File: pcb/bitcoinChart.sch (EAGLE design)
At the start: 2 parts

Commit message: Added components
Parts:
- removed U$1: PINHD-1X10, adafruit:PINHD-1X10
- added C1: (no value), resistor:C-EUC1206K
- added C6, C7: 10uF, basic_components:SMD-CAPACITOR0805
- added D1: GREEN, SparkFun-LED:LED-GREEN1206
- added D13, D14: 1n4148, basic_components:DIODESOD-323
- added D15, D16: MBR120, basic_components:DIODE-SCHOTTKYSOD-123
- added D17: RED, basic_components:LED
- added D2: RED, SparkFun-LED:LED-RED1206
- added R1, R2: (no value), resistor:R-EU_M1206
- added R15, R16, R17, R18, R19: 10K, basic_components:SMD-RESISTORR0805
- added R20: 1K, basic_components:SMD-RESISTORR0805
- added S1, S2, S3: MOMENTARY-SWITCH-SPST-PTH-6.0MM-KIT, SparkFun-Switches:MOMENTARY-SWITCH-SPST-PTH-6.0MM-KIT
- added SV1: (no value), untitled:FE10-1
- added SW5, SW6: KMR2, basic_components:BUTTON_KMR2KMR2
- added U$42: CONN-1X6, basic_components:CONN-1X6
- added U2: MPU-6050, MPU-6050:MPU-6050
- added U7: SPX3819, basic_components:MIC5219SOT-23-5
- added U8: (no value), basic_components:ESP12ESMD
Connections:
- removed net N$13: B1.D8, U$1.8
- new net +3.3V: B1.3.3V, U2.VDD
- new net 3.3V: C6.1, D17.A, R15.2, R16.2, R19.2, U7.OUT, U8.VCC
- new net ADC: U8.ADC
- new net CH_PD: R15.1, U8.CH_PD
- new net CS0: U8.CS0
- new net GPIO0: R20.1, SW6.S, SW6.S1, U8.GPIO0
- new net GPIO10: U8.*GPIO10
- new net GPIO12: U8.GPIO12
- new net GPIO13: U8.GPIO13
- new net GPIO14: U8.GPIO14
- new net GPIO15: R17.2, U8.GPIO15
- new net GPIO16: U8.GPIO16
- new net GPIO2: R19.1, U8.GPIO2
- new net GPIO4: U8.GPIO4
- new net GPIO5: U8.GPIO5
- new net GPIO9: U8.*GPIO9
- new net LDO_EN: R18.2, U7.EN
- new net MISO: U8.MISO
- new net MOSI: U8.MOSI
- new net N$1: SV1.2
- new net N$14: C7.1, D15.C, D16.C, R18.1, U7.IN
- new net N$15: D17.C, R20.2
- new net N$2: B1.A5, U2.SCL
- new net N$3: B1.A4, U2.SDA
- new net N$5: B1.D8, SV1.3
- new net RESET: D13.A, R16.1, SW5.S, SW5.S1, U8.RESET
- new net RESET_5V: D13.C
- new net RXD: B1.TX, D14.A, U8.RX
- new net RXD_5V: D14.C, U$42.3
- new net SCLK: U8.SCLK
- new net TXD: B1.RX, U$42.2, U8.TX
- new net VBAT: D16.A
- new net VIN: U$42.4
- net +5V: now also D15.A, SV1.5; no longer U$1.6, U$1.9
- net GND: now also B1.GND@0, B1.GND@1, B1.GND@2, C6.2, C7.2, R17.1, SV1.1, SW5.P, SW5.P1, SW6.P, SW6.P1, U$42.6, U2.GND, U7.GND, U8.GND; no longer U$1.10
- net N$4: now also SV1.10; no longer U$1.1
- net N$6: now also SV1.8; no longer U$1.3
- net N$7: now also SV1.7; no longer U$1.4
- net N$8: now also SV1.6; no longer U$1.5
- net N$9: now also SV1.4; no longer U$1.7

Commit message: Completed PCB
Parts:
- added C2, C4: 0.1uF, resistor:C-EUC1206K
- added C3: 10nF, resistor:C-EUC1206K
- added R3, R4, R5: 10k, resistor:R-EU_M1206
- C1: value (none) -> 2.2nF
- S1, S2, S3: value MOMENTARY-SWITCH-SPST-PTH-6.0MM-KIT -> MOMENTARY-SWITCH-SPST-SMD-6.2MM-TALL; device SparkFun-Switches:MOMENTARY-SWITCH-SPST-PTH-6.0MM-KIT -> SparkFun-Switches:MOMENTARY-SWITCH-SPST-SMD-6.2MM-TALL
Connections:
- new net LED_G: B1.*D5, R1.1
- new net LED_R: B1.*D6, R2.1
- new net N$10: C2.2, U2.REGOUT
- new net N$11: C1.2, U2.CPOUT
- new net N$12: C3.2, U2.VLOGIC
- new net N$13: D1.A, R1.2
- new net N$16: D2.A, R2.2
- new net SW1: B1.D2, R3.1, S1.1
- new net SW2: B1.D4, R4.1, S2.1
- new net SW3: B1.D7, R5.1, S3.1
- net +3.3V: now also C4.2
- net +5V: now also R3.2, R4.2, R5.2
- net GND: now also C1.1, C2.1, C3.1, C4.1, D1.C, D2.C, S1.2, S2.2, S3.2
- net N$2: now also B1.SCL; no longer B1.A5
- net N$3: now also B1.SDA; no longer B1.A4
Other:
- moved on the sheet: B1, C1, C6, C7, D1, D13, D14, D15, D16, D17, D2, R1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

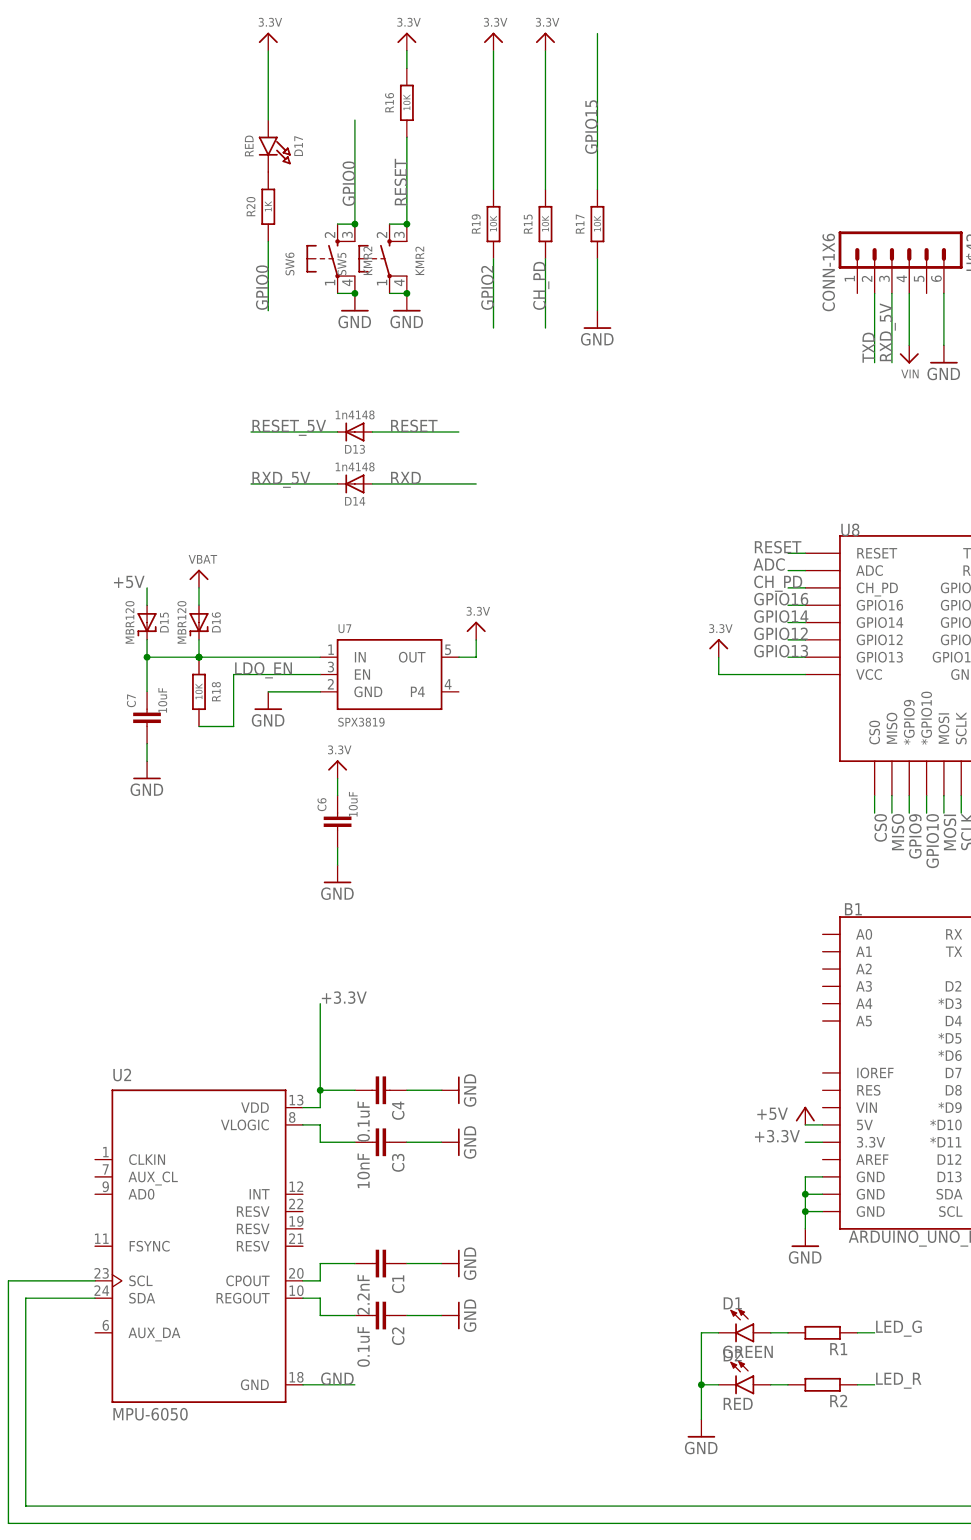
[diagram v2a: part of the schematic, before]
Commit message: Changed LED package, removed routing over antenna
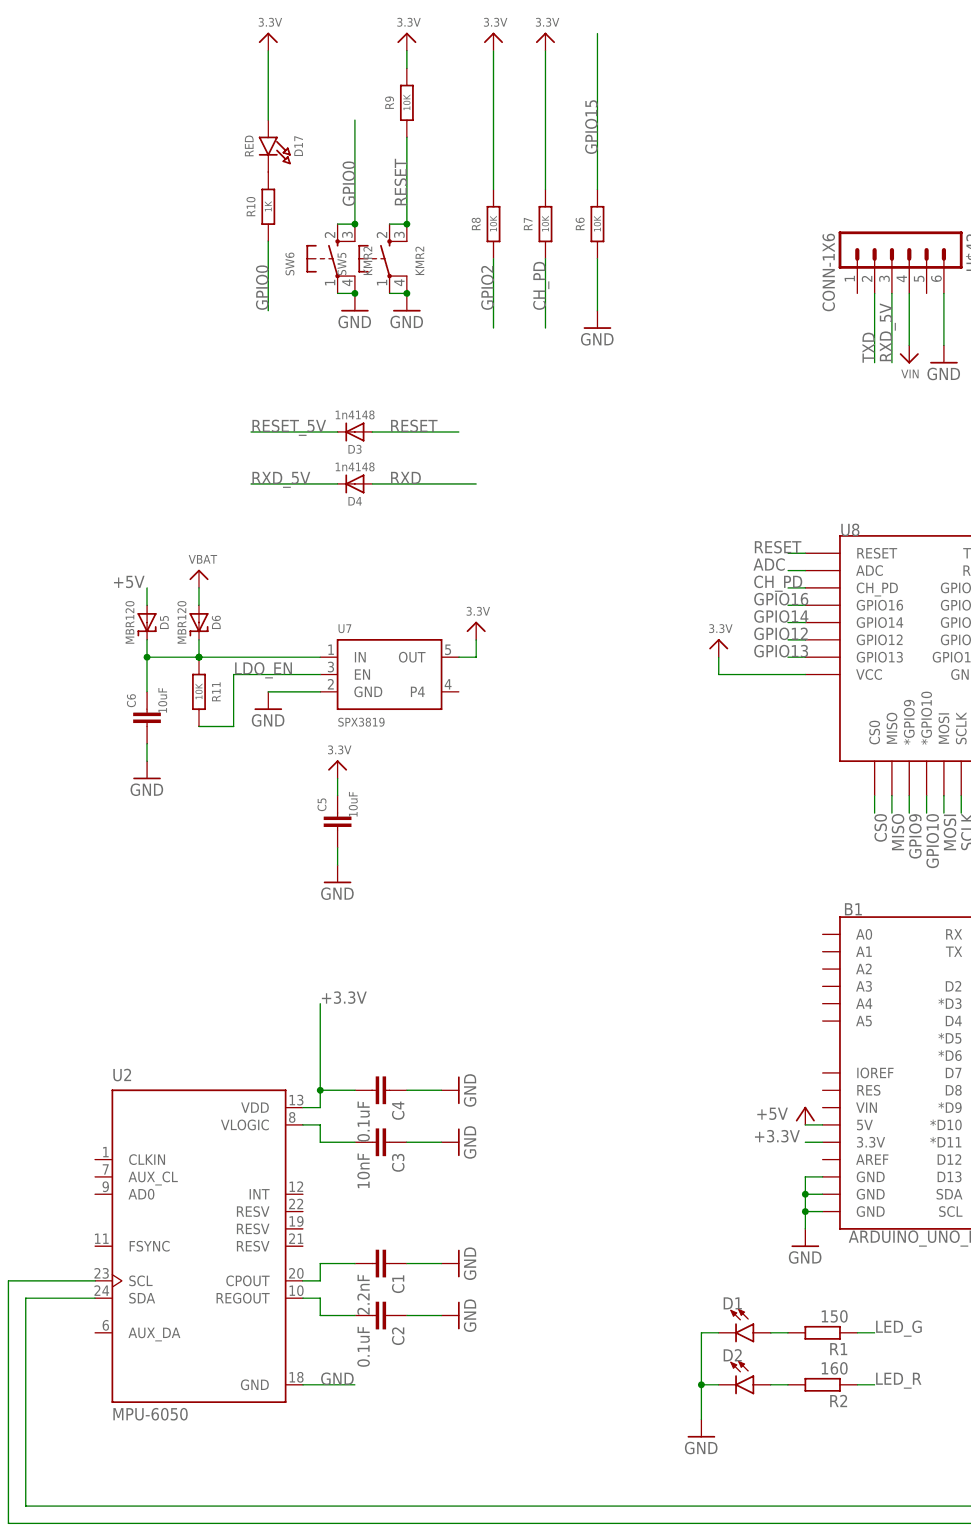
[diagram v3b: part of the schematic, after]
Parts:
- removed C7: 10uF, basic_components:SMD-CAPACITOR0805
- added C5: 10uF, basic_components:SMD-CAPACITOR0805
- D1: device SparkFun-LED:LED-GREEN1206 -> led:LEDCHIPLED_0805
- D2: device SparkFun-LED:LED-RED1206 -> led:LEDCHIPLED_0805
- R1: value (none) -> 150
- R2: value (none) -> 160
- renumbered D13 to D3, D14 to D4, D15 to D5, D16 to D6, R15 to R7, R16 to R9, R17 to R6, R18 to R11, R19 to R8, R20 to R10
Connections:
- net 3.3V: now also C5.1; no longer C6.1
- net GND: now also C5.2; no longer C7.2
- net N$14: now also C6.1; no longer C7.1
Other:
- moved on the sheet: C6

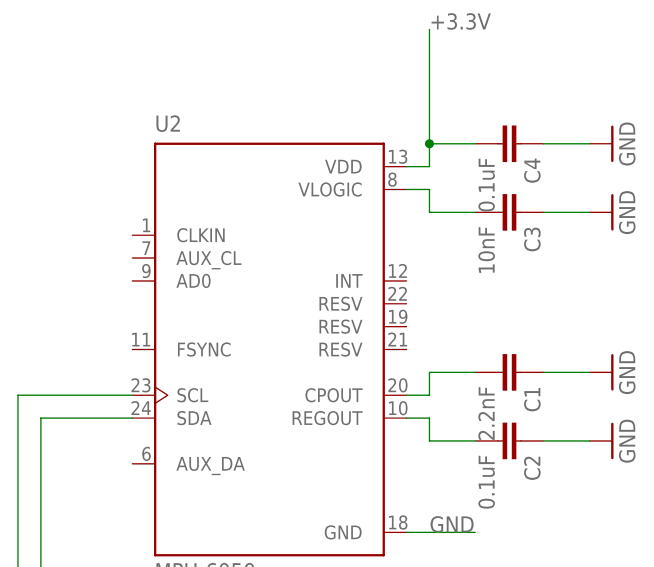
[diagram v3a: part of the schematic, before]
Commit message: Picture, connected some pins on MPU6050
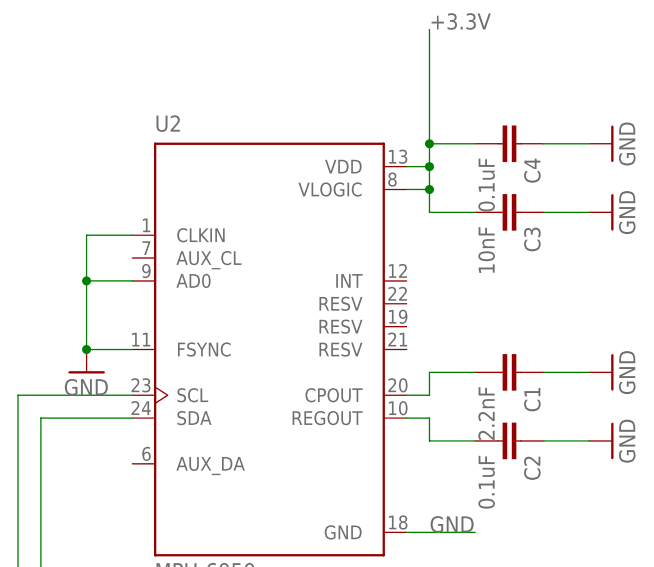
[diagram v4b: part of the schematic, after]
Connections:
- removed net N$12: C3.2, U2.VLOGIC
- net +3.3V: now also C3.2, U2.VLOGIC
- net GND: now also U2.AD0, U2.CLKIN, U2.FSYNC
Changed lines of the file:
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@@
 </class>
 <class number="1" name="test" width="0.1524" drill="0.4">
-<clearance class="1" value="0.3"/>
 </class>
 <class number="2" name="3v" width="0.1524" drill="0.3">
@@
 <part name="GND7" library="supply1" library_urn="urn:adsk.eagle:library:371" deviceset="GND" device=""/>
 <part name="FRAME1" library="frames" library_urn="urn:adsk.eagle:library:229" deviceset="A3L-LOC" device=""/>
+<part name="GND8" library="supply1" library_urn="urn:adsk.eagle:library:371" deviceset="GND" device=""/>
 </parts>
 <sheets>
@@
 <attribute name="SHEET" x="357.505" y="5.08" size="2.54" layer="94"/>
 </instance>
+<instance part="GND8" gate="1" x="48.26" y="60.96" smashed="yes">
+<attribute name="VALUE" x="45.72" y="58.42" size="1.778" layer="96"/>
+</instance>
 </instances>
 <busses>
@@
 <wire x1="248.92" y1="33.02" x2="248.92" y2="40.64" width="0.1524" layer="91"/>
 <junction x="248.92" y="33.02"/>
+</segment>
+<segment>
+<pinref part="U2" gate="G$1" pin="CLKIN"/>
+<wire x1="53.34" y1="76.2" x2="48.26" y2="76.2" width="0.1524" layer="91"/>
+<pinref part="GND8" gate="1" pin="GND"/>
+<wire x1="48.26" y1="76.2" x2="48.26" y2="71.12" width="0.1524" layer="91"/>
+<pinref part="U2" gate="G$1" pin="AD0"/>
+<wire x1="48.26" y1="71.12" x2="48.26" y2="63.5" width="0.1524" layer="91"/>
+<wire x1="53.34" y1="71.12" x2="48.26" y2="71.12" width="0.1524" layer="91"/>
+<junction x="48.26" y="71.12"/>
+<pinref part="U2" gate="G$1" pin="FSYNC"/>
+<wire x1="53.34" y1="63.5" x2="48.26" y2="63.5" width="0.1524" layer="91"/>
+<junction x="48.26" y="63.5"/>
 </segment>
 </net>
@@
 <wire x1="86.36" y1="86.36" x2="91.44" y2="86.36" width="0.1524" layer="91"/>
 <junction x="86.36" y="86.36"/>
+<pinref part="U2" gate="G$1" pin="VLOGIC"/>
+<wire x1="83.82" y1="81.28" x2="86.36" y2="81.28" width="0.1524" layer="91"/>
+<wire x1="86.36" y1="81.28" x2="86.36" y2="78.74" width="0.1524" layer="91"/>
+<pinref part="C3" gate="G$1" pin="2"/>
+<wire x1="86.36" y1="78.74" x2="91.44" y2="78.74" width="0.1524" layer="91"/>
+<wire x1="86.36" y1="81.28" x2="86.36" y2="83.82" width="0.1524" layer="91"/>
+<junction x="86.36" y="81.28"/>
+<junction x="86.36" y="83.82"/>
 </segment>
 <segment>
@@
 </segment>
 </net>
-<net name="N$12" class="0">
-<segment>
-<pinref part="U2" gate="G$1" pin="VLOGIC"/>
-<wire x1="83.82" y1="81.28" x2="86.36" y2="81.28" width="0.1524" layer="91"/>
-<wire x1="86.36" y1="81.28" x2="86.36" y2="78.74" width="0.1524" layer="91"/>
-<pinref part="C3" gate="G$1" pin="2"/>
-<wire x1="86.36" y1="78.74" x2="91.44" y2="78.74" width="0.1524" layer="91"/>
-</segment>
-</net>

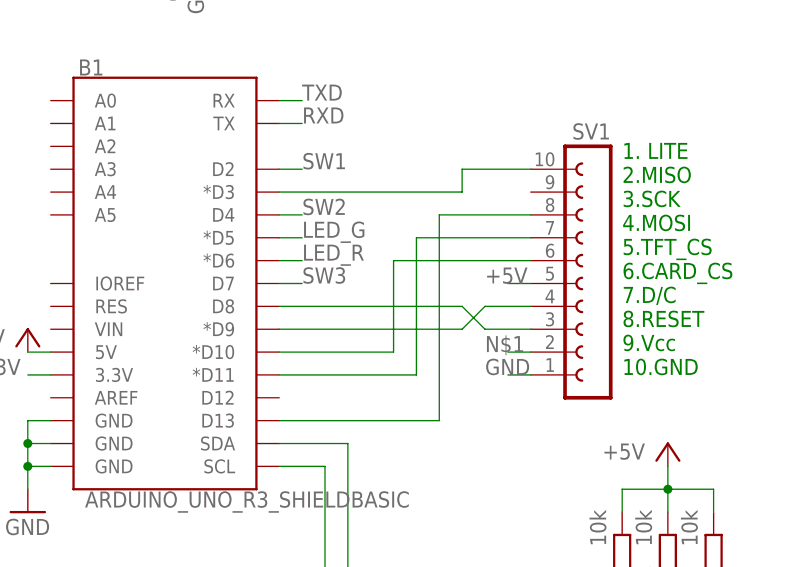
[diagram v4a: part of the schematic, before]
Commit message: Added MISO
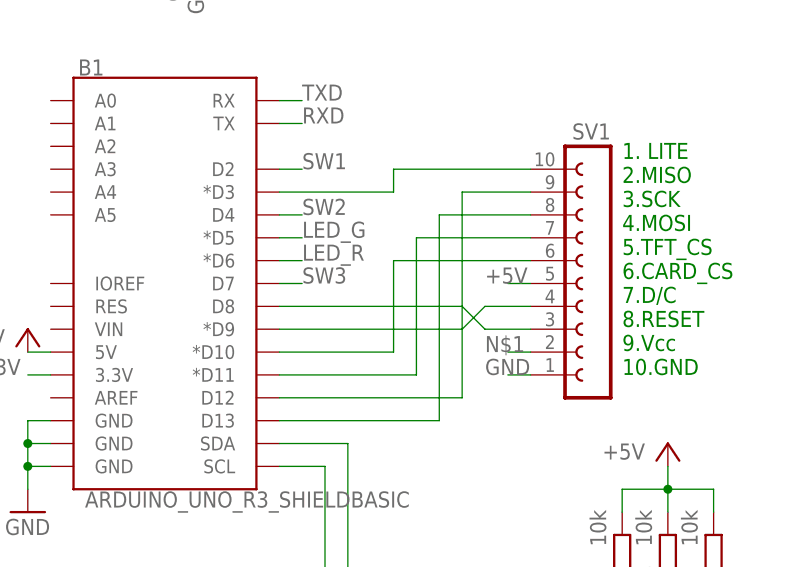
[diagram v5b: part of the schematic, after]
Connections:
- new net N$12: B1.D12, SV1.9
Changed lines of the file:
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@@
 <segment>
 <pinref part="B1" gate="G$1" pin="*D3"/>
-<wire x1="185.42" y1="99.06" x2="205.74" y2="99.06" width="0.1524" layer="91"/>
-<wire x1="205.74" y1="99.06" x2="205.74" y2="101.6" width="0.1524" layer="91"/>
-<wire x1="205.74" y1="101.6" x2="213.36" y2="101.6" width="0.1524" layer="91"/>
+<wire x1="185.42" y1="99.06" x2="198.12" y2="99.06" width="0.1524" layer="91"/>
+<wire x1="198.12" y1="99.06" x2="198.12" y2="101.6" width="0.1524" layer="91"/>
+<wire x1="198.12" y1="101.6" x2="213.36" y2="101.6" width="0.1524" layer="91"/>
 <pinref part="SV1" gate="G$1" pin="10"/>
 </segment>
@@
 </segment>
 </net>
+<net name="N$12" class="0">
+<segment>
+<pinref part="B1" gate="G$1" pin="D12"/>
+<wire x1="185.42" y1="76.2" x2="205.74" y2="76.2" width="0.1524" layer="91"/>
+<wire x1="205.74" y1="76.2" x2="205.74" y2="99.06" width="0.1524" layer="91"/>
+<pinref part="SV1" gate="G$1" pin="9"/>
+<wire x1="205.74" y1="99.06" x2="213.36" y2="99.06" width="0.1524" layer="91"/>
+</segment>
+</net>
